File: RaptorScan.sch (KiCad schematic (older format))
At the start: 5 parts, among them J1 Conn_01x01, J2 Conn_01x01, J3 Conn_01x01, J4 Conn_01x01, J5 Conn_01x01

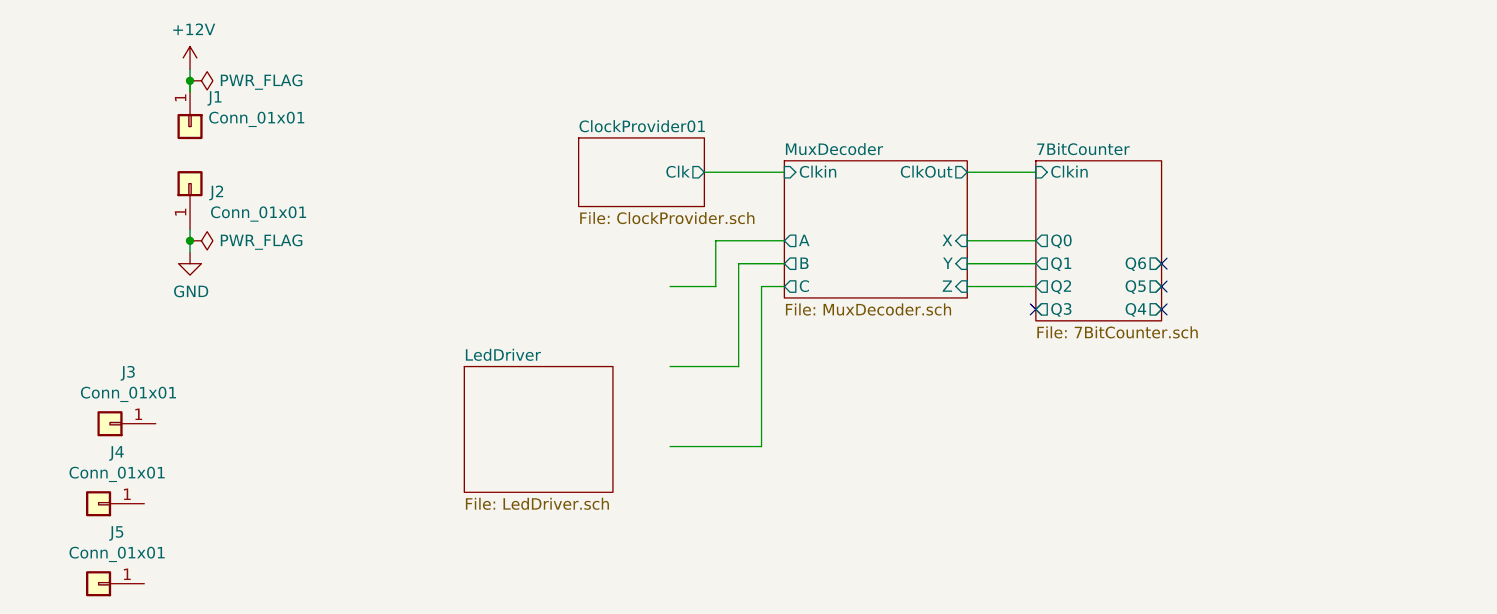
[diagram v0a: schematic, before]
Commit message: Added: Mounting holes
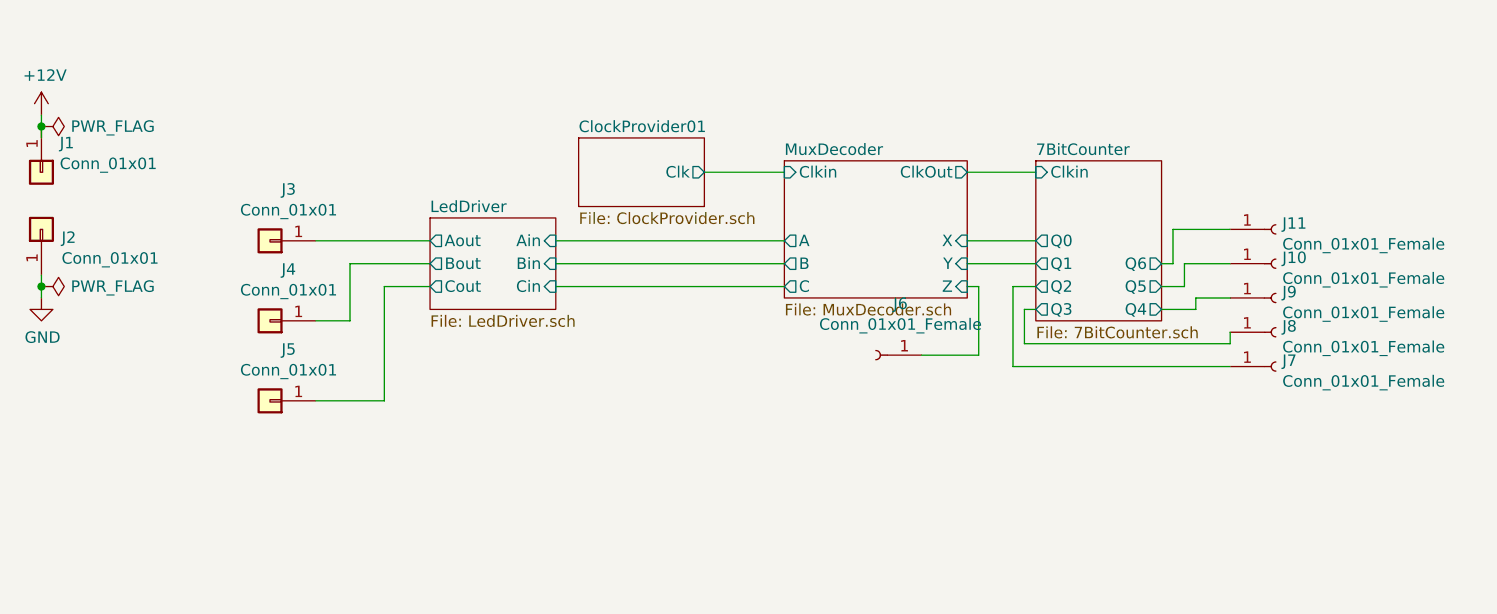
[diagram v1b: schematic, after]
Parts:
- added J10, J11, J6, J7, J8, J9: Conn_01x01_Female, TestPoint:TestPoint_THTPad_1.0x1.0mm_Drill0.5mm, symbol Connector:Conn_01x01_Female
- J1, J2, J3, J4, J5: footprint Connector_PinHeader_2.54mm:PinHeader_1x01_P2.54mm_Vertical -> MountingHole:MountingHole_2.2mm_M2_Pad
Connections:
- wire segments 18 -> 37
- no-connect marks 4 -> 0
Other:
- moved on the sheet: J1, J2, J3, J4, J5
